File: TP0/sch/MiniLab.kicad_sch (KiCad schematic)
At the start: 7 parts, among them J15 Screw_Terminal_01x06, J3 Screw_Terminal_01x06, SW9 SW_SPDT_321

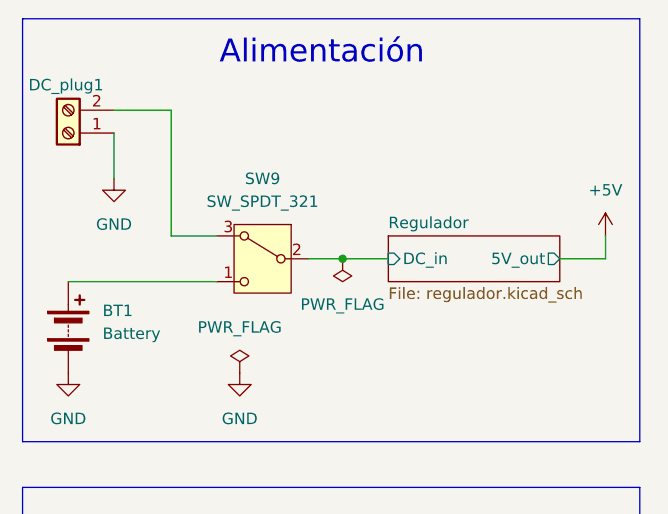
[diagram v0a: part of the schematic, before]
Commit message: Cambia llave selectora de 2 a 3 posiciones
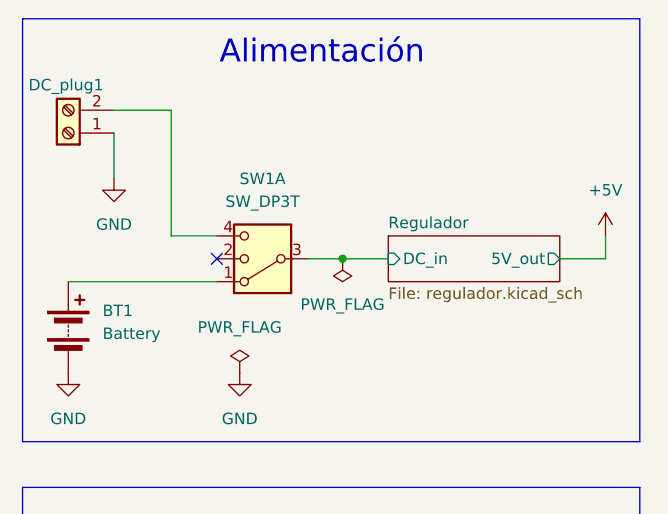
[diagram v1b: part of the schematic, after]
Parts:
- removed SW9: SW_SPDT_321, symbol Switch:SW_SPDT_321
- added SW1: SW_DP3T, symbol Switch:SW_DP3T
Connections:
- net Regulador/DC_in: now also SW1.3
- net at BT1.1 (+): now also SW1.1
- net at DC_plug1.2 (Pin_2): now also SW1.4
- no-connect marks 0 -> 1
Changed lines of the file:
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@@
 		(color 0 0 0 0)
+	)
+	(no_connect
+		(at 69.85 73.66)
 	)
 	(wire
@@
 	)
 	(symbol
-		(lib_id "Switch:SW_SPDT_321")
-		(at 74.93 73.66 0)
-		(mirror y)
-		(unit 1)
-		(body_style 1)
-		(exclude_from_sim no)
-		(in_bom yes)
-		(on_board yes)
-		(in_pos_files yes)
-		(dnp no)
-		(property "Reference" "SW9"
-			(at 74.93 64.77 0)
-			(show_name no)
-			(do_not_autoplace no)
-			(effects
-				(font
-					(size 1.27 1.27)
-				)
-			)
-		)
-		(property "Value" "SW_SPDT_321"
-			(at 74.93 67.31 0)
-			(show_name no)
-			(do_not_autoplace no)
-			(effects
-				(font
-					(size 1.27 1.27)
-				)
-			)
-		)
-		(property "Footprint" ""
-			(at 74.93 83.82 0)
-			(hide yes)
-			(show_name no)
-			(do_not_autoplace no)
-			(effects
-				(font
-					(size 1.27 1.27)
-				)
-			)
-		)
-		(property "Datasheet" ""
-			(at 74.93 81.28 0)
-			(hide yes)
-			(show_name no)
-			(do_not_autoplace no)
-			(effects
-				(font
-					(size 1.27 1.27)
-				)
-			)
-		)
-		(property "Description" "Switch, single pole double throw"
-			(at 74.93 73.66 0)
-			(hide yes)
-			(show_name no)
-			(do_not_autoplace no)
-			(effects
-				(font
-					(size 1.27 1.27)
-				)
-			)
-		)
-		(pin "3"
-		)
-		(pin "2"
-		)
-		(pin "1"
-		)
-		(instances
-			(project "MiniLab"
-				(path "/9d7a1f0f-be2a-4650-bdfd-79562484ee87"
-					(reference "SW9")
-					(unit 1)
-				)
-			)
-		)
-	)
-	(symbol
 		(lib_id "Connector:Screw_Terminal_01x02")
 		(at 226.06 68.58 0)
@@
 					(unit 1)
 				)
+			)
+		)
+	)
+	(symbol
+		(lib_id "Switch:SW_DP3T")
+		(at 74.93 73.66 180)
+		(unit 1)
+		(body_style 1)
+		(exclude_from_sim no)
+		(in_bom yes)
+		(on_board yes)
+		(in_pos_files yes)
+		(dnp no)
+		(fields_autoplaced yes)
+		(property "Reference" "SW1"
+			(at 74.93 64.77 0)
+			(show_name no)
+			(do_not_autoplace no)
+			(effects
+				(font
+					(size 1.27 1.27)
+				)
+			)
+		)
+		(property "Value" "SW_DP3T"
+			(at 74.93 67.31 0)
+			(show_name no)
+			(do_not_autoplace no)
+			(effects
+				(font
+					(size 1.27 1.27)
+				)
+			)
+		)
+		(property "Footprint" ""
+			(at 90.805 78.105 0)
+			(hide yes)
+			(show_name no)
+			(do_not_autoplace no)
+			(effects
+				(font
+					(size 1.27 1.27)
+				)
+			)
+		)
+		(property "Datasheet" ""
+			(at 90.805 78.105 0)
+			(hide yes)
+			(show_name no)
+			(do_not_autoplace no)
+			(effects
+				(font
+					(size 1.27 1.27)
+				)
+			)
+		)
+		(property "Description" "Switch, three position, dual pole triple throw, 3 position switch, SP3T"
+			(at 74.93 73.66 0)
+			(hide yes)
+			(show_name no)
+			(do_not_autoplace no)
+			(effects
+				(font
+					(size 1.27 1.27)
+				)
+			)
+		)
+		(pin "6"
+		)
+		(pin "3"
+		)
+		(pin "1"
+		)
+		(pin "2"
+		)
+		(pin "4"
+		)
+		(pin "5"
+		)
+		(pin "7"
+		)
+		(pin "8"
+		)
+		(instances
+			(project "MiniLab"
+				(path "/9d7a1f0f-be2a-4650-bdfd-79562484ee87"
+					(reference "SW1")
+					(unit 1)
+				)
